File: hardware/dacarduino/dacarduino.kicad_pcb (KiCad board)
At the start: 2 copper layers, 98 x 98 mm, 98 parts, among them J1 Conn_01x03_Male, J10 Conn_01x02, J11 GATE IN, J12 GATE IN, J13 GATE IN, J14 GATE IN, J15 CV IN, J16 CV IN, J17 CV IN, J18 CV IN, J19 Conn_01x01, J2 Conn_01x03_Male, J20 Conn_01x01, J21 Conn_01x01, J22 Conn_01x01, J23 Conn_01x01, J24 Conn_01x01, J25 Conn_01x01, J26 Conn_01x01, J27 Conn_01x01, J28 Conn_01x01, J29 Conn_01x01, J3 Molex 2 pin, J30 Conn_01x01, J31 Conn_01x01, J32 Conn_01x01, J33 Conn_01x01, J34 Conn_01x01, J4 Molex 2 pin, J5 Molex 2 pin, J6 Molex 2 pin, J7 VCC, J8 EURO_PWR_2x5, J9 Conn_01x04, Q1 2N3904, Q2 2N3904, Q3 2N3904, Q4 2N3904, Q5 2N3904, Q6 2N3904, U1 MCP4922, U2 TL072, U3 REF02CP+, U4 SN74LS154N

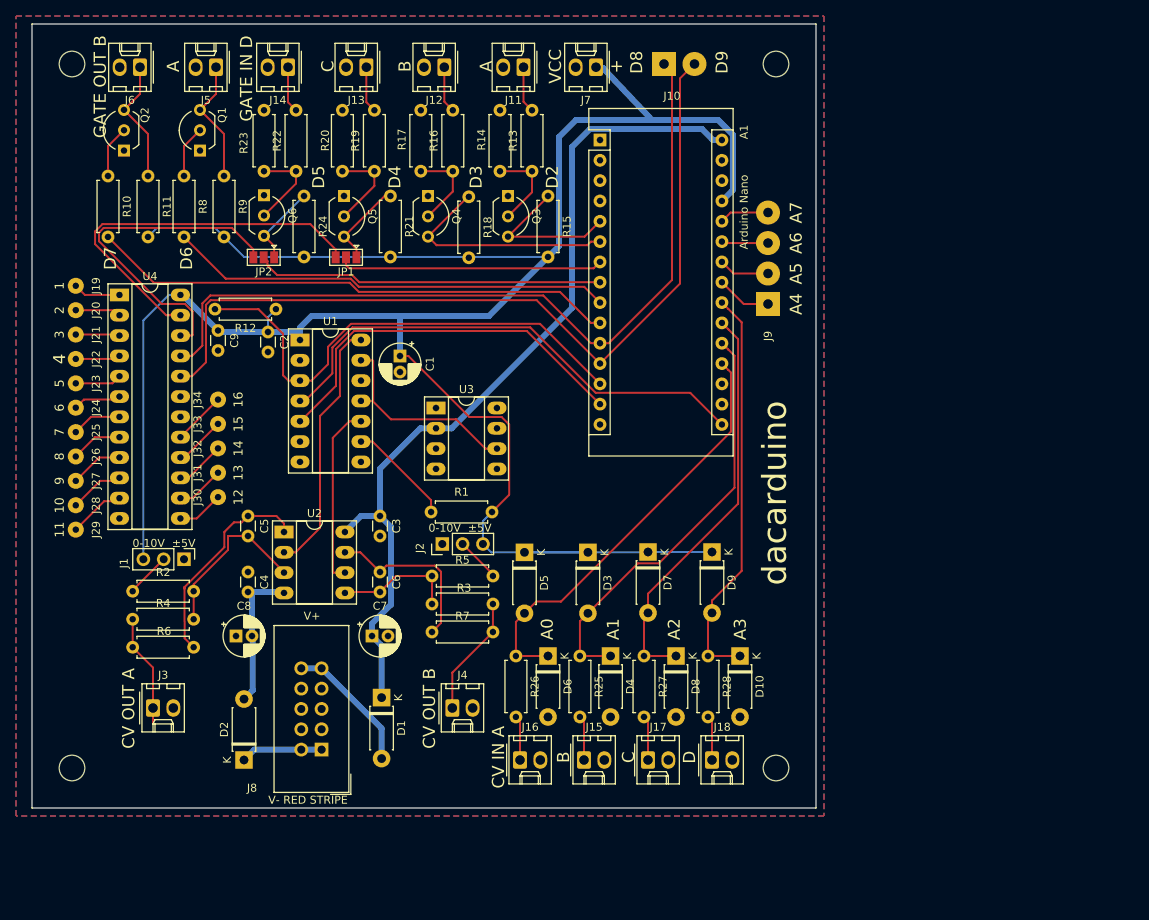
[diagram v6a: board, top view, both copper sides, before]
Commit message: Revert multiplexer idea
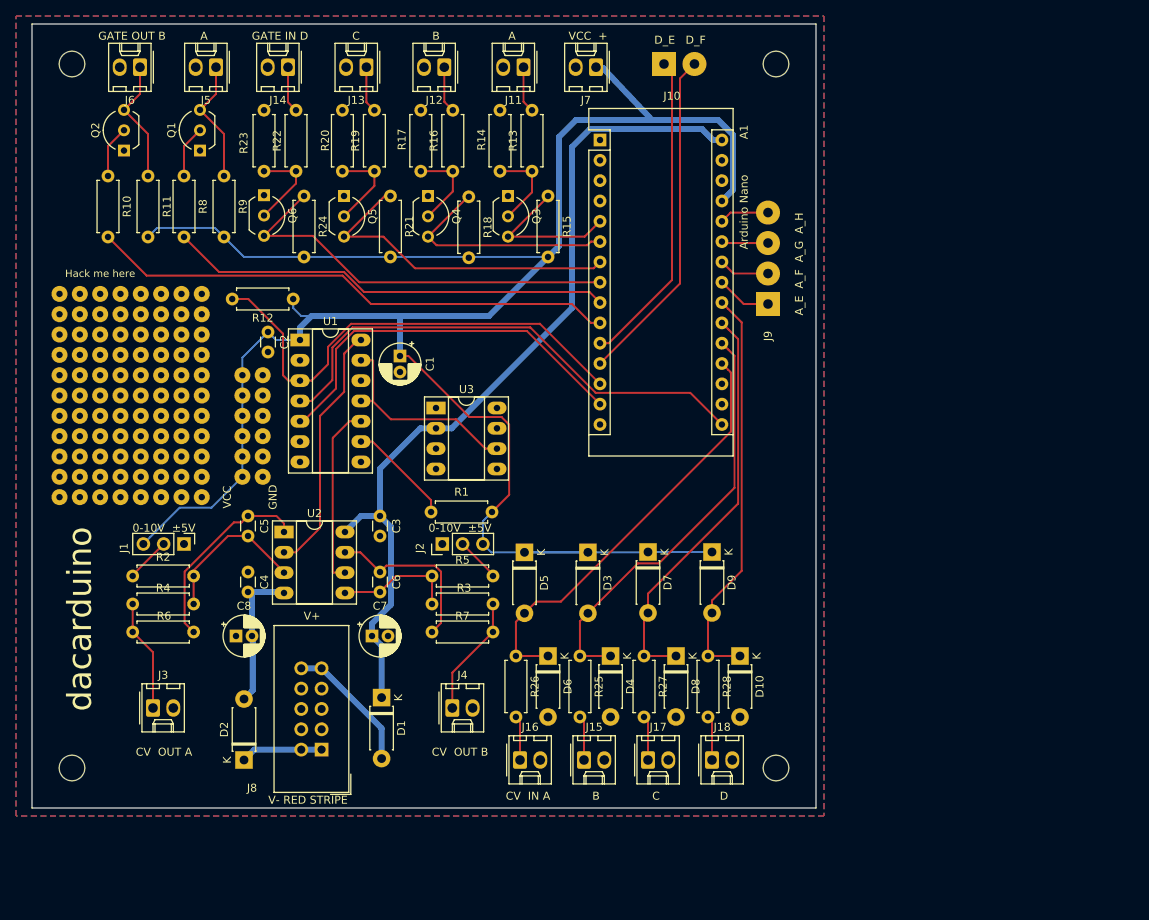
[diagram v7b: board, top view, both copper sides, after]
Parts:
- removed C9: 0.1uF, Capacitor_THT:C_Disc_D3.0mm_W1.6mm_P2.50mm
- removed J19, J20, J21, J22, J23, J24, J25, J26, J27, J28, J29, J30, J31, J32, J33, J34: Conn_01x01, Connector_Wire:SolderWirePad_1x01_Drill0.8mm
- removed JP1, JP2: SolderJumper_3_Open, Jumper:SolderJumper-3_P1.3mm_Open_Pad1.0x1.5mm
- removed U4: SN74LS154N, Package_DIP:DIP-24_W7.62mm_Socket_LongPads
- added REF**: SolderWirePad_1x01_Drill0.8mm, Connector_Wire:SolderWirePad_1x01_Drill0.8mm, F.Cu at (106.7, 81.3)
- added REF**: SolderWirePad_1x01_Drill0.8mm, Connector_Wire:SolderWirePad_1x01_Drill0.8mm, F.Cu at (116.8, 88.9)
- added REF**: SolderWirePad_1x01_Drill0.8mm, Connector_Wire:SolderWirePad_1x01_Drill0.8mm, F.Cu at (94.0, 86.4)
- added REF**: SolderWirePad_1x01_Drill0.8mm, Connector_Wire:SolderWirePad_1x01_Drill0.8mm, F.Cu at (116.8, 101.6)
- added REF**: SolderWirePad_1x01_Drill0.8mm, Connector_Wire:SolderWirePad_1x01_Drill0.8mm, F.Cu at (116.8, 91.4)
- added REF**: SolderWirePad_1x01_Drill0.8mm, Connector_Wire:SolderWirePad_1x01_Drill0.8mm, F.Cu at (116.8, 99.1)
- added REF**: SolderWirePad_1x01_Drill0.8mm, Connector_Wire:SolderWirePad_1x01_Drill0.8mm, F.Cu at (116.8, 94.0)
- added REF**: SolderWirePad_1x01_Drill0.8mm, Connector_Wire:SolderWirePad_1x01_Drill0.8mm, F.Cu at (116.8, 96.5)
- added REF**: SolderWirePad_1x01_Drill0.8mm, Connector_Wire:SolderWirePad_1x01_Drill0.8mm, F.Cu at (101.6, 78.7)
- added REF**: SolderWirePad_1x01_Drill0.8mm, Connector_Wire:SolderWirePad_1x01_Drill0.8mm, F.Cu at (101.6, 81.3)
- added REF**: SolderWirePad_1x01_Drill0.8mm, Connector_Wire:SolderWirePad_1x01_Drill0.8mm, F.Cu at (101.6, 83.8)
- added REF**: SolderWirePad_1x01_Drill0.8mm, Connector_Wire:SolderWirePad_1x01_Drill0.8mm, F.Cu at (91.4, 78.7)
- added REF**: SolderWirePad_1x01_Drill0.8mm, Connector_Wire:SolderWirePad_1x01_Drill0.8mm, F.Cu at (104.1, 81.3)
- added REF**: SolderWirePad_1x01_Drill0.8mm, Connector_Wire:SolderWirePad_1x01_Drill0.8mm, F.Cu at (96.5, 78.7)
- added REF**: SolderWirePad_1x01_Drill0.8mm, Connector_Wire:SolderWirePad_1x01_Drill0.8mm, F.Cu at (99.1, 78.7)
- added REF**: SolderWirePad_1x01_Drill0.8mm, Connector_Wire:SolderWirePad_1x01_Drill0.8mm, F.Cu at (94.0, 78.7)
- added REF**: SolderWirePad_1x01_Drill0.8mm, Connector_Wire:SolderWirePad_1x01_Drill0.8mm, F.Cu at (91.4, 81.3)
- added REF**: SolderWirePad_1x01_Drill0.8mm, Connector_Wire:SolderWirePad_1x01_Drill0.8mm, F.Cu at (96.5, 81.3)
- added REF**: SolderWirePad_1x01_Drill0.8mm, Connector_Wire:SolderWirePad_1x01_Drill0.8mm, F.Cu at (94.0, 81.3)
- added REF**: SolderWirePad_1x01_Drill0.8mm, Connector_Wire:SolderWirePad_1x01_Drill0.8mm, F.Cu at (99.1, 81.3)
- added REF**: SolderWirePad_1x01_Drill0.8mm, Connector_Wire:SolderWirePad_1x01_Drill0.8mm, F.Cu at (94.0, 83.8)
- added REF**: SolderWirePad_1x01_Drill0.8mm, Connector_Wire:SolderWirePad_1x01_Drill0.8mm, F.Cu at (99.1, 83.8)
- added REF**: SolderWirePad_1x01_Drill0.8mm, Connector_Wire:SolderWirePad_1x01_Drill0.8mm, F.Cu at (96.5, 83.8)
- added REF**: SolderWirePad_1x01_Drill0.8mm, Connector_Wire:SolderWirePad_1x01_Drill0.8mm, F.Cu at (104.1, 83.8)
- added REF**: SolderWirePad_1x01_Drill0.8mm, Connector_Wire:SolderWirePad_1x01_Drill0.8mm, F.Cu at (91.4, 83.8)
- added REF**: SolderWirePad_1x01_Drill0.8mm, Connector_Wire:SolderWirePad_1x01_Drill0.8mm, F.Cu at (114.3, 99.1)
- added REF**: SolderWirePad_1x01_Drill0.8mm, Connector_Wire:SolderWirePad_1x01_Drill0.8mm, F.Cu at (114.3, 101.6)
- added REF**: SolderWirePad_1x01_Drill0.8mm, Connector_Wire:SolderWirePad_1x01_Drill0.8mm, F.Cu at (114.3, 94.0)
- added REF**: SolderWirePad_1x01_Drill0.8mm, Connector_Wire:SolderWirePad_1x01_Drill0.8mm, F.Cu at (114.3, 96.5)
- added REF**: SolderWirePad_1x01_Drill0.8mm, Connector_Wire:SolderWirePad_1x01_Drill0.8mm, F.Cu at (114.3, 91.4)
- added REF**: SolderWirePad_1x01_Drill0.8mm, Connector_Wire:SolderWirePad_1x01_Drill0.8mm, F.Cu at (114.3, 88.9)
- added REF**: SolderWirePad_1x01_Drill0.8mm, Connector_Wire:SolderWirePad_1x01_Drill0.8mm, F.Cu at (101.6, 104.1)
- added REF**: SolderWirePad_1x01_Drill0.8mm, Connector_Wire:SolderWirePad_1x01_Drill0.8mm, F.Cu at (104.1, 104.1)
- added REF**: SolderWirePad_1x01_Drill0.8mm, Connector_Wire:SolderWirePad_1x01_Drill0.8mm, F.Cu at (99.1, 104.1)
- added REF**: SolderWirePad_1x01_Drill0.8mm, Connector_Wire:SolderWirePad_1x01_Drill0.8mm, F.Cu at (106.7, 83.8)
- added REF**: SolderWirePad_1x01_Drill0.8mm, Connector_Wire:SolderWirePad_1x01_Drill0.8mm, F.Cu at (91.4, 104.1)
- added REF**: SolderWirePad_1x01_Drill0.8mm, Connector_Wire:SolderWirePad_1x01_Drill0.8mm, F.Cu at (94.0, 104.1)
- added REF**: SolderWirePad_1x01_Drill0.8mm, Connector_Wire:SolderWirePad_1x01_Drill0.8mm, F.Cu at (106.7, 104.1)
- added REF**: SolderWirePad_1x01_Drill0.8mm, Connector_Wire:SolderWirePad_1x01_Drill0.8mm, F.Cu at (109.2, 104.1)
- added REF**: SolderWirePad_1x01_Drill0.8mm, Connector_Wire:SolderWirePad_1x01_Drill0.8mm, F.Cu at (96.5, 104.1)
- added REF**: SolderWirePad_1x01_Drill0.8mm, Connector_Wire:SolderWirePad_1x01_Drill0.8mm, F.Cu at (99.1, 101.6)
- added REF**: SolderWirePad_1x01_Drill0.8mm, Connector_Wire:SolderWirePad_1x01_Drill0.8mm, F.Cu at (104.1, 101.6)
- added REF**: SolderWirePad_1x01_Drill0.8mm, Connector_Wire:SolderWirePad_1x01_Drill0.8mm, F.Cu at (91.4, 101.6)
- added REF**: SolderWirePad_1x01_Drill0.8mm, Connector_Wire:SolderWirePad_1x01_Drill0.8mm, F.Cu at (106.7, 101.6)
- added REF**: SolderWirePad_1x01_Drill0.8mm, Connector_Wire:SolderWirePad_1x01_Drill0.8mm, F.Cu at (109.2, 101.6)
- added REF**: SolderWirePad_1x01_Drill0.8mm, Connector_Wire:SolderWirePad_1x01_Drill0.8mm, F.Cu at (109.2, 83.8)
- added REF**: SolderWirePad_1x01_Drill0.8mm, Connector_Wire:SolderWirePad_1x01_Drill0.8mm, F.Cu at (96.5, 101.6)
- added REF**: SolderWirePad_1x01_Drill0.8mm, Connector_Wire:SolderWirePad_1x01_Drill0.8mm, F.Cu at (94.0, 101.6)
- added REF**: SolderWirePad_1x01_Drill0.8mm, Connector_Wire:SolderWirePad_1x01_Drill0.8mm, F.Cu at (101.6, 101.6)
- added REF**: SolderWirePad_1x01_Drill0.8mm, Connector_Wire:SolderWirePad_1x01_Drill0.8mm, F.Cu at (104.1, 99.1)
- added REF**: SolderWirePad_1x01_Drill0.8mm, Connector_Wire:SolderWirePad_1x01_Drill0.8mm, F.Cu at (106.7, 99.1)
- added REF**: SolderWirePad_1x01_Drill0.8mm, Connector_Wire:SolderWirePad_1x01_Drill0.8mm, F.Cu at (94.0, 99.1)
- added REF**: SolderWirePad_1x01_Drill0.8mm, Connector_Wire:SolderWirePad_1x01_Drill0.8mm, F.Cu at (91.4, 99.1)
- added REF**: SolderWirePad_1x01_Drill0.8mm, Connector_Wire:SolderWirePad_1x01_Drill0.8mm, F.Cu at (101.6, 99.1)
- added REF**: SolderWirePad_1x01_Drill0.8mm, Connector_Wire:SolderWirePad_1x01_Drill0.8mm, F.Cu at (99.1, 99.1)
- added REF**: SolderWirePad_1x01_Drill0.8mm, Connector_Wire:SolderWirePad_1x01_Drill0.8mm, F.Cu at (96.5, 99.1)
- added REF**: SolderWirePad_1x01_Drill0.8mm, Connector_Wire:SolderWirePad_1x01_Drill0.8mm, F.Cu at (109.2, 81.3)
- added REF**: SolderWirePad_1x01_Drill0.8mm, Connector_Wire:SolderWirePad_1x01_Drill0.8mm, F.Cu at (109.2, 99.1)
- added REF**: SolderWirePad_1x01_Drill0.8mm, Connector_Wire:SolderWirePad_1x01_Drill0.8mm, F.Cu at (101.6, 96.5)
- added REF**: SolderWirePad_1x01_Drill0.8mm, Connector_Wire:SolderWirePad_1x01_Drill0.8mm, F.Cu at (109.2, 96.5)
- added REF**: SolderWirePad_1x01_Drill0.8mm, Connector_Wire:SolderWirePad_1x01_Drill0.8mm, F.Cu at (96.5, 96.5)
- added REF**: SolderWirePad_1x01_Drill0.8mm, Connector_Wire:SolderWirePad_1x01_Drill0.8mm, F.Cu at (91.4, 96.5)
- added REF**: SolderWirePad_1x01_Drill0.8mm, Connector_Wire:SolderWirePad_1x01_Drill0.8mm, F.Cu at (104.1, 96.5)
- added REF**: SolderWirePad_1x01_Drill0.8mm, Connector_Wire:SolderWirePad_1x01_Drill0.8mm, F.Cu at (106.7, 96.5)
- added REF**: SolderWirePad_1x01_Drill0.8mm, Connector_Wire:SolderWirePad_1x01_Drill0.8mm, F.Cu at (99.1, 96.5)
- added REF**: SolderWirePad_1x01_Drill0.8mm, Connector_Wire:SolderWirePad_1x01_Drill0.8mm, F.Cu at (94.0, 96.5)
- added REF**: SolderWirePad_1x01_Drill0.8mm, Connector_Wire:SolderWirePad_1x01_Drill0.8mm, F.Cu at (94.0, 94.0)
- added REF**: SolderWirePad_1x01_Drill0.8mm, Connector_Wire:SolderWirePad_1x01_Drill0.8mm, F.Cu at (109.2, 78.7)
- added REF**: SolderWirePad_1x01_Drill0.8mm, Connector_Wire:SolderWirePad_1x01_Drill0.8mm, F.Cu at (96.5, 94.0)
- added REF**: SolderWirePad_1x01_Drill0.8mm, Connector_Wire:SolderWirePad_1x01_Drill0.8mm, F.Cu at (109.2, 94.0)
- added REF**: SolderWirePad_1x01_Drill0.8mm, Connector_Wire:SolderWirePad_1x01_Drill0.8mm, F.Cu at (101.6, 94.0)
- added REF**: SolderWirePad_1x01_Drill0.8mm, Connector_Wire:SolderWirePad_1x01_Drill0.8mm, F.Cu at (91.4, 94.0)
- added REF**: SolderWirePad_1x01_Drill0.8mm, Connector_Wire:SolderWirePad_1x01_Drill0.8mm, F.Cu at (106.7, 94.0)
- added REF**: SolderWirePad_1x01_Drill0.8mm, Connector_Wire:SolderWirePad_1x01_Drill0.8mm, F.Cu at (99.1, 94.0)
- added REF**: SolderWirePad_1x01_Drill0.8mm, Connector_Wire:SolderWirePad_1x01_Drill0.8mm, F.Cu at (104.1, 94.0)
- added REF**: SolderWirePad_1x01_Drill0.8mm, Connector_Wire:SolderWirePad_1x01_Drill0.8mm, F.Cu at (106.7, 91.4)
- added REF**: SolderWirePad_1x01_Drill0.8mm, Connector_Wire:SolderWirePad_1x01_Drill0.8mm, F.Cu at (91.4, 91.4)
- added REF**: SolderWirePad_1x01_Drill0.8mm, Connector_Wire:SolderWirePad_1x01_Drill0.8mm, F.Cu at (104.1, 91.4)
- added REF**: SolderWirePad_1x01_Drill0.8mm, Connector_Wire:SolderWirePad_1x01_Drill0.8mm, F.Cu at (106.7, 78.7)
- added REF**: SolderWirePad_1x01_Drill0.8mm, Connector_Wire:SolderWirePad_1x01_Drill0.8mm, F.Cu at (94.0, 91.4)
- added REF**: SolderWirePad_1x01_Drill0.8mm, Connector_Wire:SolderWirePad_1x01_Drill0.8mm, F.Cu at (109.2, 91.4)
- added REF**: SolderWirePad_1x01_Drill0.8mm, Connector_Wire:SolderWirePad_1x01_Drill0.8mm, F.Cu at (96.5, 91.4)
- added REF**: SolderWirePad_1x01_Drill0.8mm, Connector_Wire:SolderWirePad_1x01_Drill0.8mm, F.Cu at (99.1, 91.4)
- added REF**: SolderWirePad_1x01_Drill0.8mm, Connector_Wire:SolderWirePad_1x01_Drill0.8mm, F.Cu at (101.6, 91.4)
- added REF**: SolderWirePad_1x01_Drill0.8mm, Connector_Wire:SolderWirePad_1x01_Drill0.8mm, F.Cu at (94.0, 88.9)
- added REF**: SolderWirePad_1x01_Drill0.8mm, Connector_Wire:SolderWirePad_1x01_Drill0.8mm, F.Cu at (106.7, 88.9)
- added REF**: SolderWirePad_1x01_Drill0.8mm, Connector_Wire:SolderWirePad_1x01_Drill0.8mm, F.Cu at (99.1, 88.9)
- added REF**: SolderWirePad_1x01_Drill0.8mm, Connector_Wire:SolderWirePad_1x01_Drill0.8mm, F.Cu at (109.2, 88.9)
- added REF**: SolderWirePad_1x01_Drill0.8mm, Connector_Wire:SolderWirePad_1x01_Drill0.8mm, F.Cu at (96.5, 88.9)
- added REF**: SolderWirePad_1x01_Drill0.8mm, Connector_Wire:SolderWirePad_1x01_Drill0.8mm, F.Cu at (104.1, 78.7)
- added REF**: SolderWirePad_1x01_Drill0.8mm, Connector_Wire:SolderWirePad_1x01_Drill0.8mm, F.Cu at (101.6, 88.9)
- added REF**: SolderWirePad_1x01_Drill0.8mm, Connector_Wire:SolderWirePad_1x01_Drill0.8mm, F.Cu at (91.4, 88.9)
- added REF**: SolderWirePad_1x01_Drill0.8mm, Connector_Wire:SolderWirePad_1x01_Drill0.8mm, F.Cu at (104.1, 88.9)
- added REF**: SolderWirePad_1x01_Drill0.8mm, Connector_Wire:SolderWirePad_1x01_Drill0.8mm, F.Cu at (91.4, 86.4)
- added REF**: SolderWirePad_1x01_Drill0.8mm, Connector_Wire:SolderWirePad_1x01_Drill0.8mm, F.Cu at (109.2, 86.4)
- added REF**: SolderWirePad_1x01_Drill0.8mm, Connector_Wire:SolderWirePad_1x01_Drill0.8mm, F.Cu at (106.7, 86.4)
- added REF**: SolderWirePad_1x01_Drill0.8mm, Connector_Wire:SolderWirePad_1x01_Drill0.8mm, F.Cu at (104.1, 86.4)
- added REF**: SolderWirePad_1x01_Drill0.8mm, Connector_Wire:SolderWirePad_1x01_Drill0.8mm, F.Cu at (101.6, 86.4)
- added REF**: SolderWirePad_1x01_Drill0.8mm, Connector_Wire:SolderWirePad_1x01_Drill0.8mm, F.Cu at (99.1, 86.4)
- added REF**: SolderWirePad_1x01_Drill0.8mm, Connector_Wire:SolderWirePad_1x01_Drill0.8mm, F.Cu at (96.5, 86.4)
- moved R12 2.50 mm to (120.7, 79.4)
- moved J1 1.91 mm to (107.0, 110.0)
- moved R2 1.91 mm to (100.6, 114.0)
- moved R4 1.91 mm to (108.2, 117.5)
- moved R6 1.91 mm to (108.2, 121.0)
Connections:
- net /Arduino/A0 renamed /Arduino/A_IN_A
- net /Arduino/A1 renamed /Arduino/A_IN_B
- net /Arduino/A2 renamed /Arduino/A_IN_C
- net /Arduino/A3 renamed /Arduino/A_IN_D
- net /Arduino/A4 renamed /Arduino/A_IN_E
- net /Arduino/A5 renamed /Arduino/A_IN_F
- net /Arduino/A6 renamed /Arduino/A_IN_G
- net /Arduino/A7 renamed /Arduino/A_IN_H
- net /Arduino/D2 renamed /Arduino/D_IN_A
- net /Arduino/D3 renamed /Arduino/D_IN_B
- net /Arduino/D6 renamed /Arduino/D_OUT_A
- net /Arduino/D7 renamed /Arduino/D_OUT_B
- net /Arduino/D8 renamed /Arduino/D_IN_E
- net /Arduino/D9 renamed /Arduino/D_IN_F
- A1 pad 7: /Arduino/D4 -> /Arduino/D_IN_C
- A1 pad 8: /Arduino/D5 -> /Arduino/D_IN_D
- Q5 pad 3: /Inputs/Gate in C/D_IN -> /Arduino/D_IN_C
- Q6 pad 3: /Inputs/Gate in D/D_IN -> /Arduino/D_IN_D
- R21 pad 1: /Inputs/Gate in C/D_IN -> /Arduino/D_IN_C
- R24 pad 1: /Inputs/Gate in D/D_IN -> /Arduino/D_IN_D
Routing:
- net /Arduino/D_IN_F: track 106.2 -> 42.3 mm
- net /Arduino/D_IN_E: track 100.8 -> 39.7 mm
- net /Arduino/D_IN_D: track 0.00 -> 51.5 mm
- net Net-(JP1-Pad3): track 49.6 -> 0.00 mm
- net /Arduino/D5: track 43.6 -> 0.00 mm
- net Net-(JP2-Pad3): track 42.5 -> 0.00 mm
- net /Arduino/D_IN_C: track 0.00 -> 41.9 mm
- net /Arduino/D4: track 33.2 -> 0.00 mm
- net VCC: track 279.5 -> 266.1 mm
- net /Inputs/Gate in C/D_IN: track 11.1 -> 0.00 mm
- net /Inputs/Gate in D/D_IN: track 10.3 -> 0.00 mm
- net Net-(J29-Pad1): track 7.09 -> 0.00 mm
- net Net-(J28-Pad1): track 6.88 -> 0.00 mm
- net Net-(J27-Pad1): track 6.67 -> 0.00 mm
- net Net-(J34-Pad1): track 6.65 -> 0.00 mm
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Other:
- board text added: "A_E A_F A_G A_H"
- board text added: "D_E D_F"
- board text added: "GND"
- board text added: "Hack me here"
- board text added: "VCC +"
- board text removed: "+"
- board text removed: "1"
- board text removed: "10"
- board text removed: "11"
- board text removed: "12"
- board text removed: "13"
- board text removed: "14"
- board text removed: "15"
- board text removed: "16"
- board text removed: "2"
- board text removed: "3"
- board text removed: "4"
- board text removed: "5"
- board text removed: "6"
- board text removed: "7"
- board text removed: "8"
- board text removed: "9"
- board text removed: "A0"
- board text removed: "A1"
- board text removed: "A2"
- board text removed: "A3"
- board text removed: "A4"
- board text removed: "A5"
- board text removed: "A6"
- board text removed: "A7"
- board text removed: "D2"
- board text removed: "D3"
- board text removed: "D4"
- board text removed: "D5"
- board text removed: "D6"
- board text removed: "D7"
- board text removed: "D8"
- board text removed: "D9"
